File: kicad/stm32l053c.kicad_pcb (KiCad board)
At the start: 2 copper layers, 90 x 70 mm, 57 parts, among them J1 Water_Level, J2 Motion, J3 Door, J4 Door_Led, J6 Pump, J7 BATTERY, P1 SWD, Q1 Q_NMOS_GSD, Q2 Q_PMOS_GSD, SW1 SW_Push_SPDT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

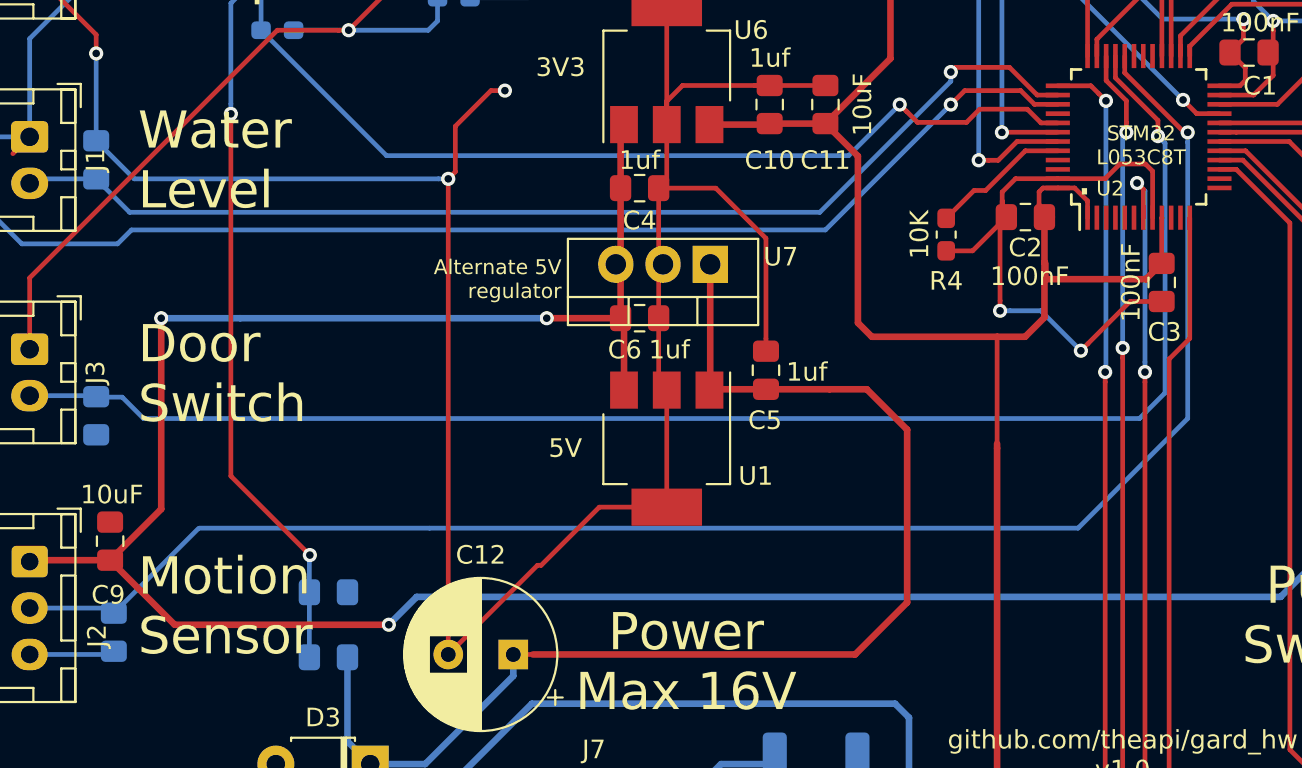
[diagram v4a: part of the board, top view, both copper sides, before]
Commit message: Heatsinking for the 5V regulator
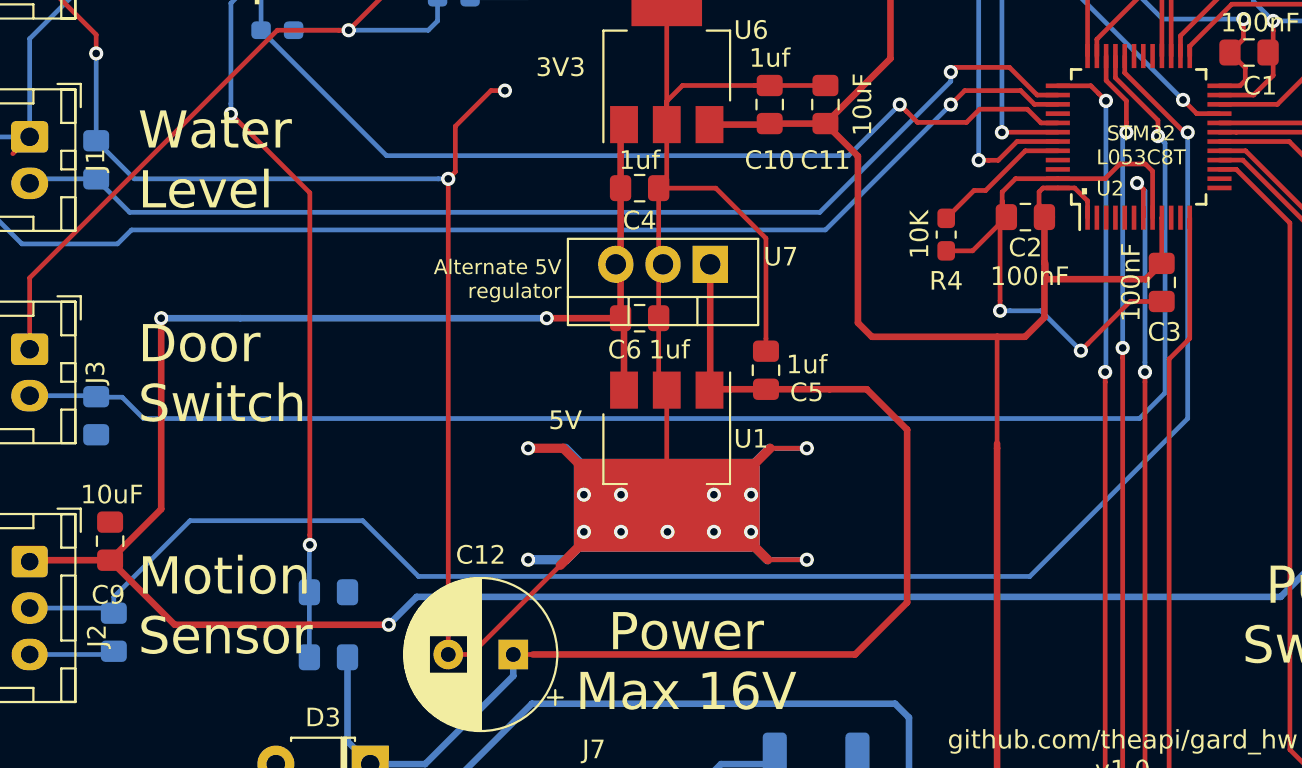
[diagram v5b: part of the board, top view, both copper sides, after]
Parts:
- U1: footprint Package_TO_SOT_SMD:SOT-223-3_TabPin2 -> theapi:SOT-223-3_TabPin2_heatsink
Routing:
- net Earth: track 461.2 -> 520.3 mm, vias 12 -> 25
- net MOTION: track 87.7 -> 90.8 mm

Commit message: Logos
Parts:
- added REF**: TheApiLogoTiny, theapi:TheApiLogoTiny, F.Cu at (97.0, 114.5)
- added REF**: TheApiLogo, theapi:TheApiLogoSmall, F.Cu at (148.5, 99.0)
- added REF**: TheApiLogo, theapi:TheApiLogo, B.Cu at (157.5, 90.5)
- moved C8 4.20 mm to (134.0, 62.5)
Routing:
- net DIO0: track 19.6 -> 28.4 mm
- net Earth: track 520.3 -> 522.5 mm, vias 25 -> 28
- net +3V3: track 220.8 -> 222.4 mm
- net DOOR: track 81.4 -> 80.7 mm
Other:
- board text added: "github.com/theapi/gard_hw Jan 2019 v1.0"
- board text removed: "github.com/theapi/gard_hw v1.0"

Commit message: Name on the board
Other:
- board text added: "G.A.R.D."
- board text added: "Garden Animal Repellent Device"
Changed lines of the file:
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@@
   (general
     (thickness 1.6)
-    (drawings 43)
+    (drawings 45)
     (tracks 580)
     (zones 0)
@@
     (fp_line (start 2.575 -21.95) (end 3.3 -20.725) (layer B.SilkS) (width 0.15))
   )
+  (gr_text "Garden\nAnimal\nRepellent\nDevice" (at 165.25 72.25) (layer B.SilkS)
+    (effects (font (size 5 4) (thickness 1)) (justify left mirror))
+  )
+  (gr_text G.A.R.D. (at 149 95) (layer F.SilkS)
+    (effects (font (size 5 4) (thickness 1)))
+  )
   (gr_text "Alternate 5V\nregulator" (at 118.8 86.4) (layer F.SilkS)

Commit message: Gerbers
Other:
- rule solder_mask_min_width: 0.25 -> 0.05
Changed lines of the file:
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@@
     (pad_drill 0.762)
     (pad_to_mask_clearance 0.2)
-    (solder_mask_min_width 0.25)
+    (solder_mask_min_width 0.05)
     (aux_axis_origin 0 0)
     (visible_elements FFFFFF7F)
     (pcbplotparams
-      (layerselection 0x010f0_80000001)
+      (layerselection 0x010f0_ffffffff)
       (usegerberextensions true)
       (usegerberattributes false)
